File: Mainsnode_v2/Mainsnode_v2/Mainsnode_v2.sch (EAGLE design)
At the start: 38 parts, among them J2 WIRE_HOLE-14AWG, J3 WIRE_HOLE-14AWG, U1 ATUM, U2 ADE7753, X1 ECS-35-17-5PX-TR

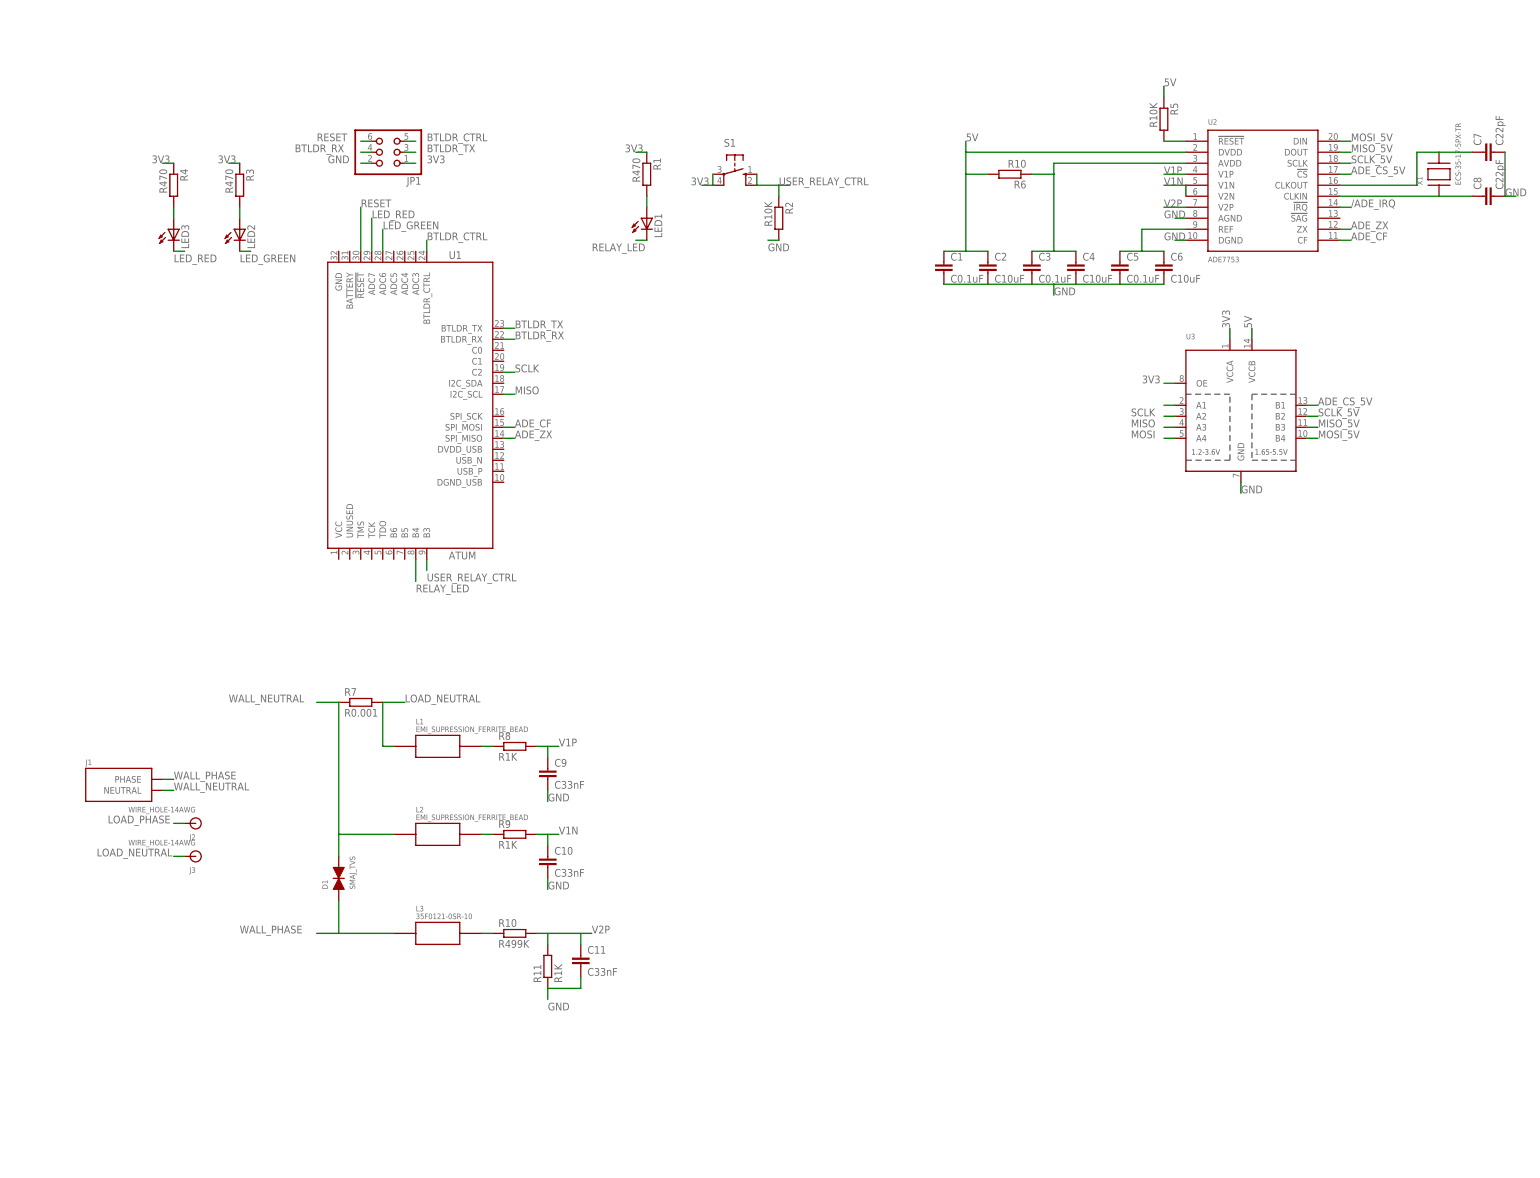
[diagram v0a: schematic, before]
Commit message: Finish schematic, start PCB
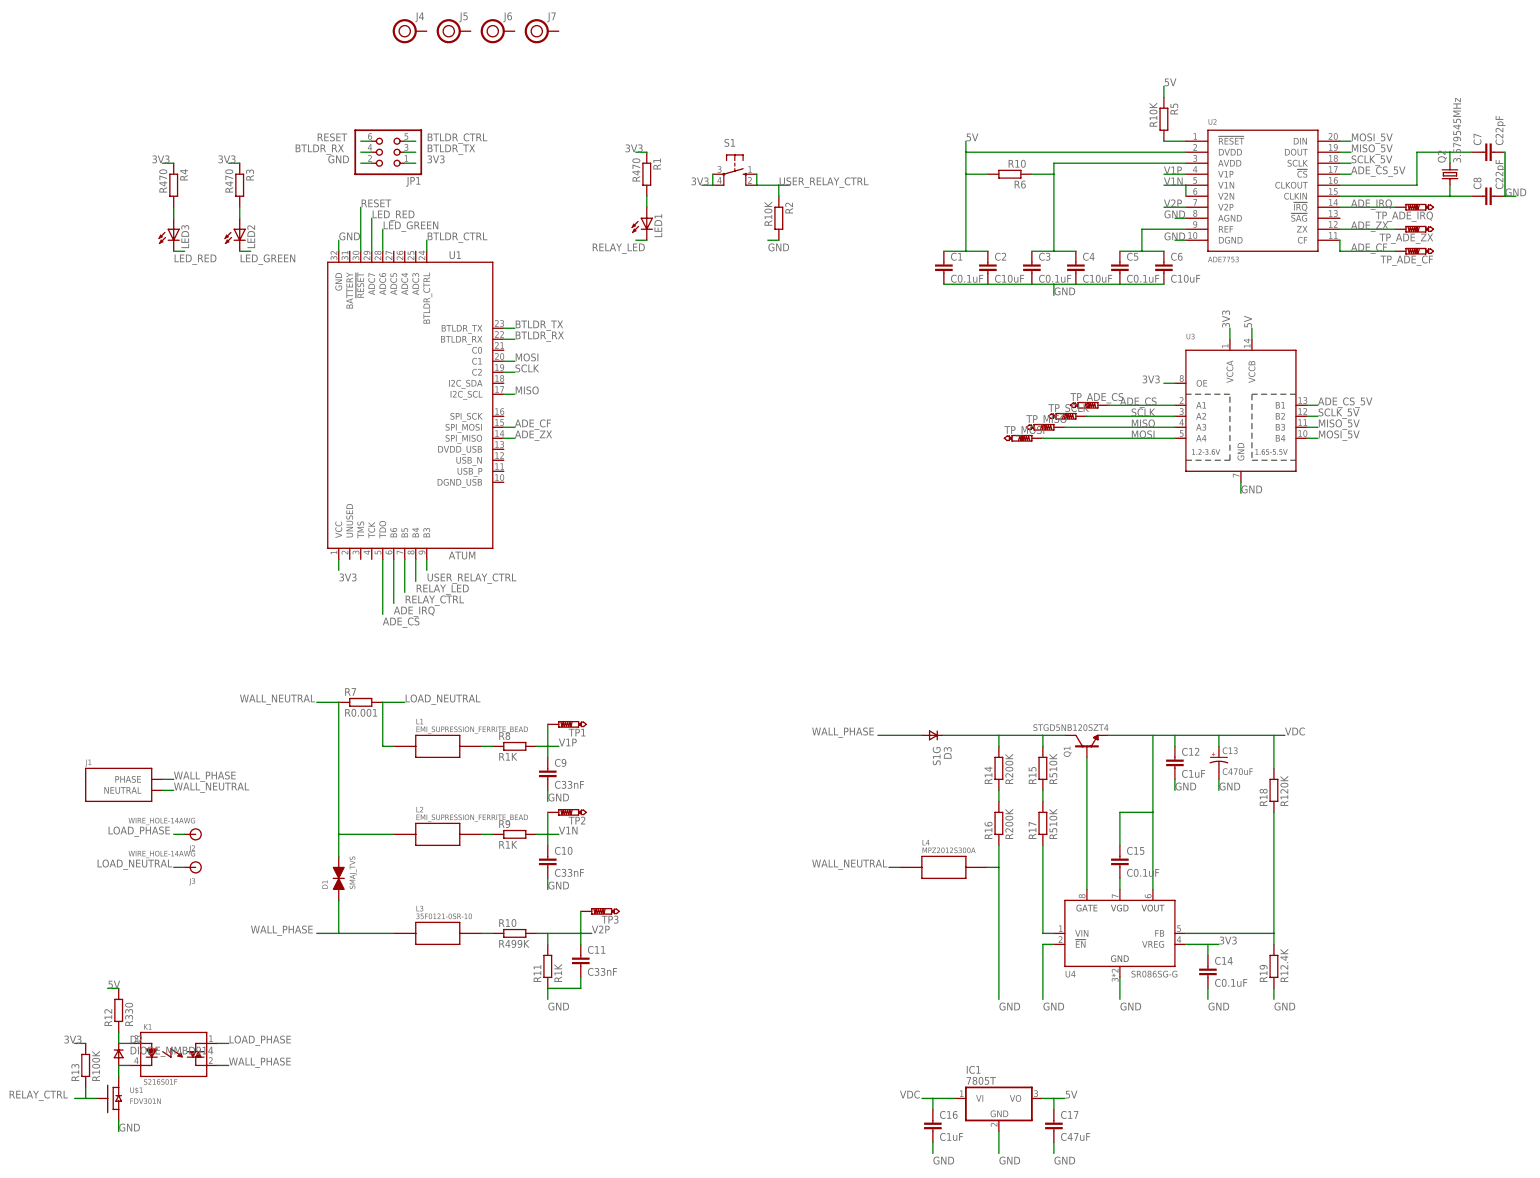
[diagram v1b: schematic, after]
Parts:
- removed X1: ECS-35-17-5PX-TR, powercube:ECS-35-17-5PX-TR
- added C12, C16: C1uF, resistor:C-EUC0805
- added C13: C470uF, powercube:CAP_EEE-FP1E471AP
- added C14, C15: C0.1uF, resistor:C-EUC0805
- added C17: C47uF, resistor:C-EUC0805
- added D2: DIODE_MMBD914, powercube:DIODE_MMBD914
- added D3: S1G, powercube:S1G
- added IC1: 7805T, adafruit:7805T
- added J4, J5, J6, J7: HOLE, powercube:HOLE
- added K1: S216S01F, powercube:S216S01F
- added L4: MPZ2012S300A, powercube:MPZ2012S300A
- added Q1: STGD5NB120SZT4, powercube:STGD5NB120SZT4
- added Q2: 3.579545MHz, crystal:CRYSTALHC49S
- added R12: R330, resistor:R-EU_R0805
- added R13: R100K, resistor:R-EU_R0805
- added R14, R16: R200K, resistor:R-EU_R0805
- added R15, R17: R510K, resistor:R-EU_R0805
- added R18: R120K, resistor:R-EU_R0805
- added R19: R12.4K, resistor:R-EU_R0805
- added TP1, TP2, TP3, TP_ADE_CF, TP_ADE_CS, TP_ADE_IRQ, TP_ADE_ZX, TP_MISO, TP_MOSI, TP_SCLK: PTR1PAD1-13, testpad:PTR1PAD1-13
- added U$1: FDV301N, powercube:FDV301N
- added U4: SR086SG-G, powercube:SR086SG-G
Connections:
- removed net /ADE_IRQ: U2.!IRQ
- removed net N$6: U3.A1
- new net ADE_CS: TP_ADE_CS.TP, U1.TDO, U3.A1
- new net ADE_IRQ: TP_ADE_IRQ.TP, U1.B6, U2.!IRQ
- new net N$11: D2.CATHODE, K1.3, R12.1
- new net N$12: D2.ANNODE, K1.4, U$1.D
- new net N$13: D3.CATHODE, Q1.C, R14.2, R15.2
- new net N$14: R14.1, R16.2
- new net N$15: R15.1, R17.2
- new net N$17: R17.1, U4.VIN
- new net N$18: Q1.G, U4.GATE
- new net N$21: C15.2, U4.VGD
- new net N$23: R18.1, R19.2, U4.FB
- new net RELAY_CTRL: R13.1, U$1.G, U1.B5
- new net VDC: C12.1, C13.+, C15.1, C16.1, IC1.VI, Q1.E, R18.2, U4.VOUT
- net 3V3: now also C14.1, R13.2, U1.VCC, U4.VREG
- net 5V: now also C17.1, IC1.VO, R12.2
- net ADE_CF: now also TP_ADE_CF.TP
- net ADE_ZX: now also TP_ADE_ZX.TP
- net GND: now also C12.2, C13.-, C14.2, C16.2, C17.2, IC1.GND, L4.P$2, R16.1, R19.1, U$1.S, U1.GND, U4.!EN, U4.GND
- net LOAD_PHASE: now also K1.1
- net MISO: now also TP_MISO.TP
- net MOSI: now also TP_MOSI.TP, U1.C1
- net N$19: now also Q2.2; no longer X1.P$2
- net N$20: now also Q2.1; no longer X1.P$1
- net SCLK: now also TP_SCLK.TP
- net V1N: now also TP2.TP
- net V1P: now also TP1.TP
- net V2P: now also TP3.TP
- net WALL_NEUTRAL: now also L4.P$1
- net WALL_PHASE: now also D3.ANNODE, K1.2
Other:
- note added: "5V Regulator"
- note added: "AC DC Converter"
- note added: "AC Plug"
- note added: "Load Control Relay"
- moved on the sheet: J2, J3
